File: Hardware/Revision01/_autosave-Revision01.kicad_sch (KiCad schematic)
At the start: 24 parts, among them J1 Battery connector, SW1 ON/OFF_SW_SPST_LED, U1 NUCLEO-L476RG

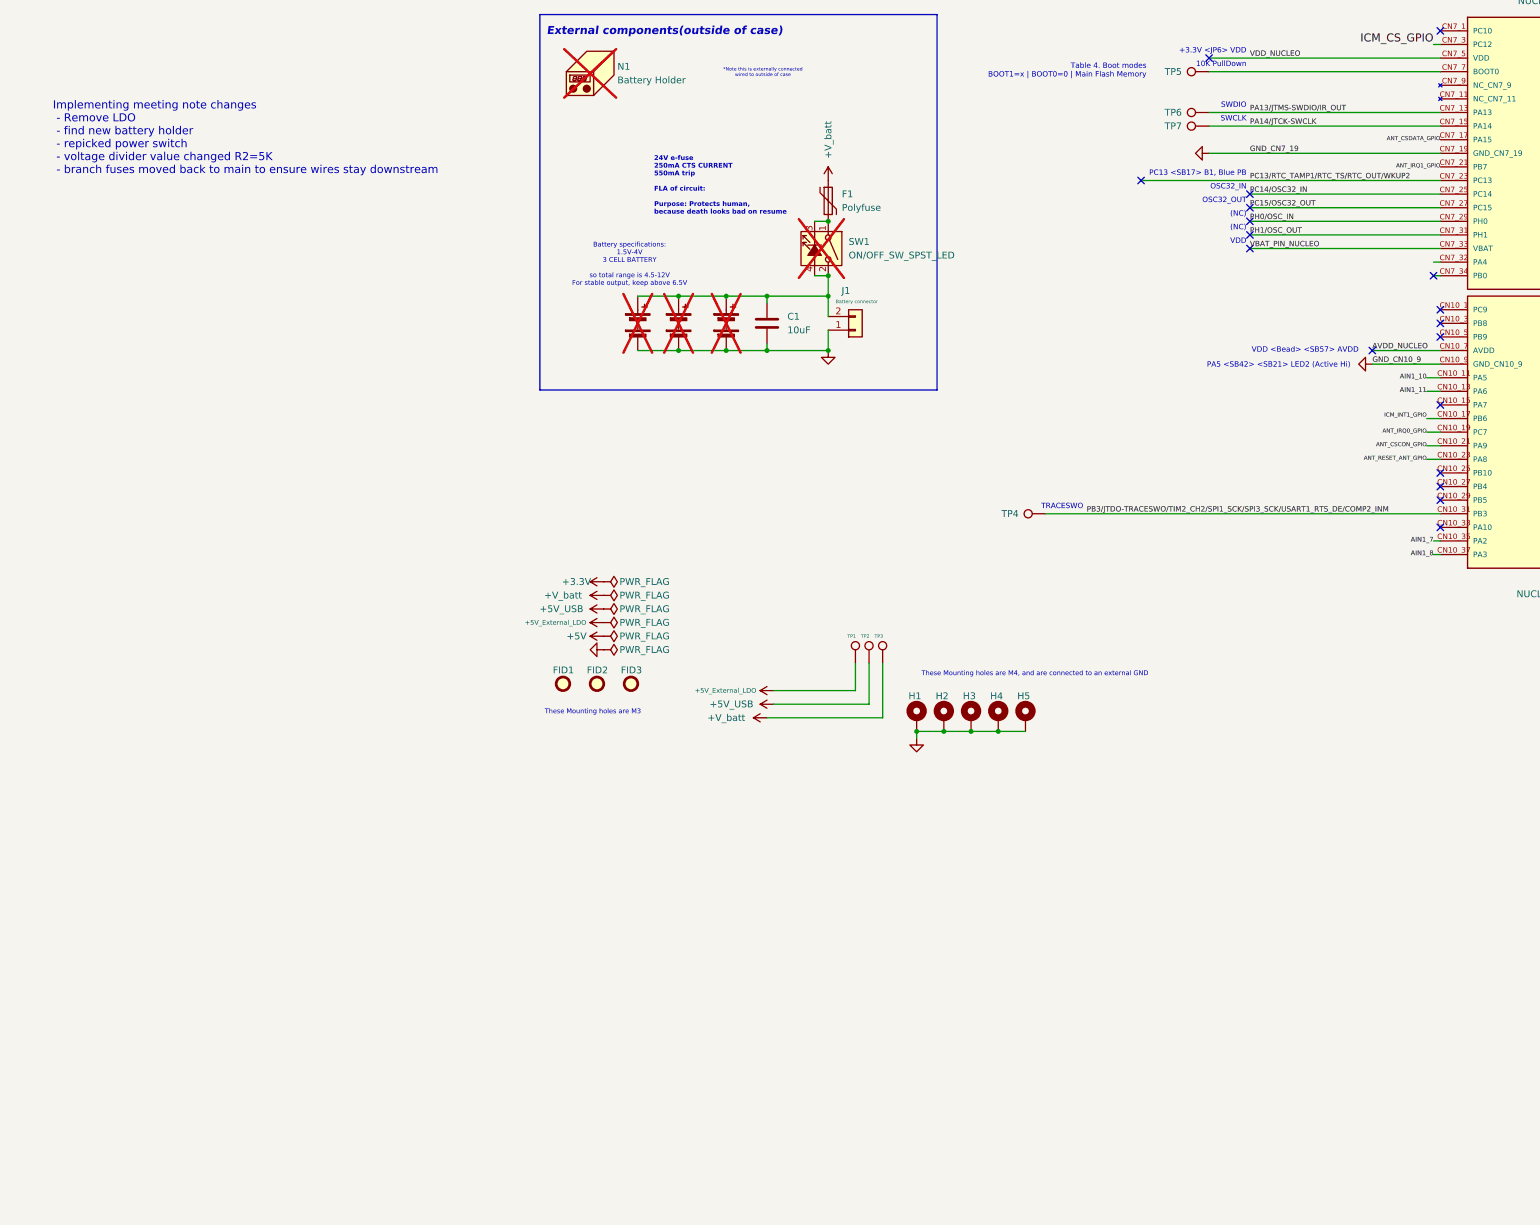
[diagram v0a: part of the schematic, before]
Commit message: Small details on PART B, restarting component placement on PART A
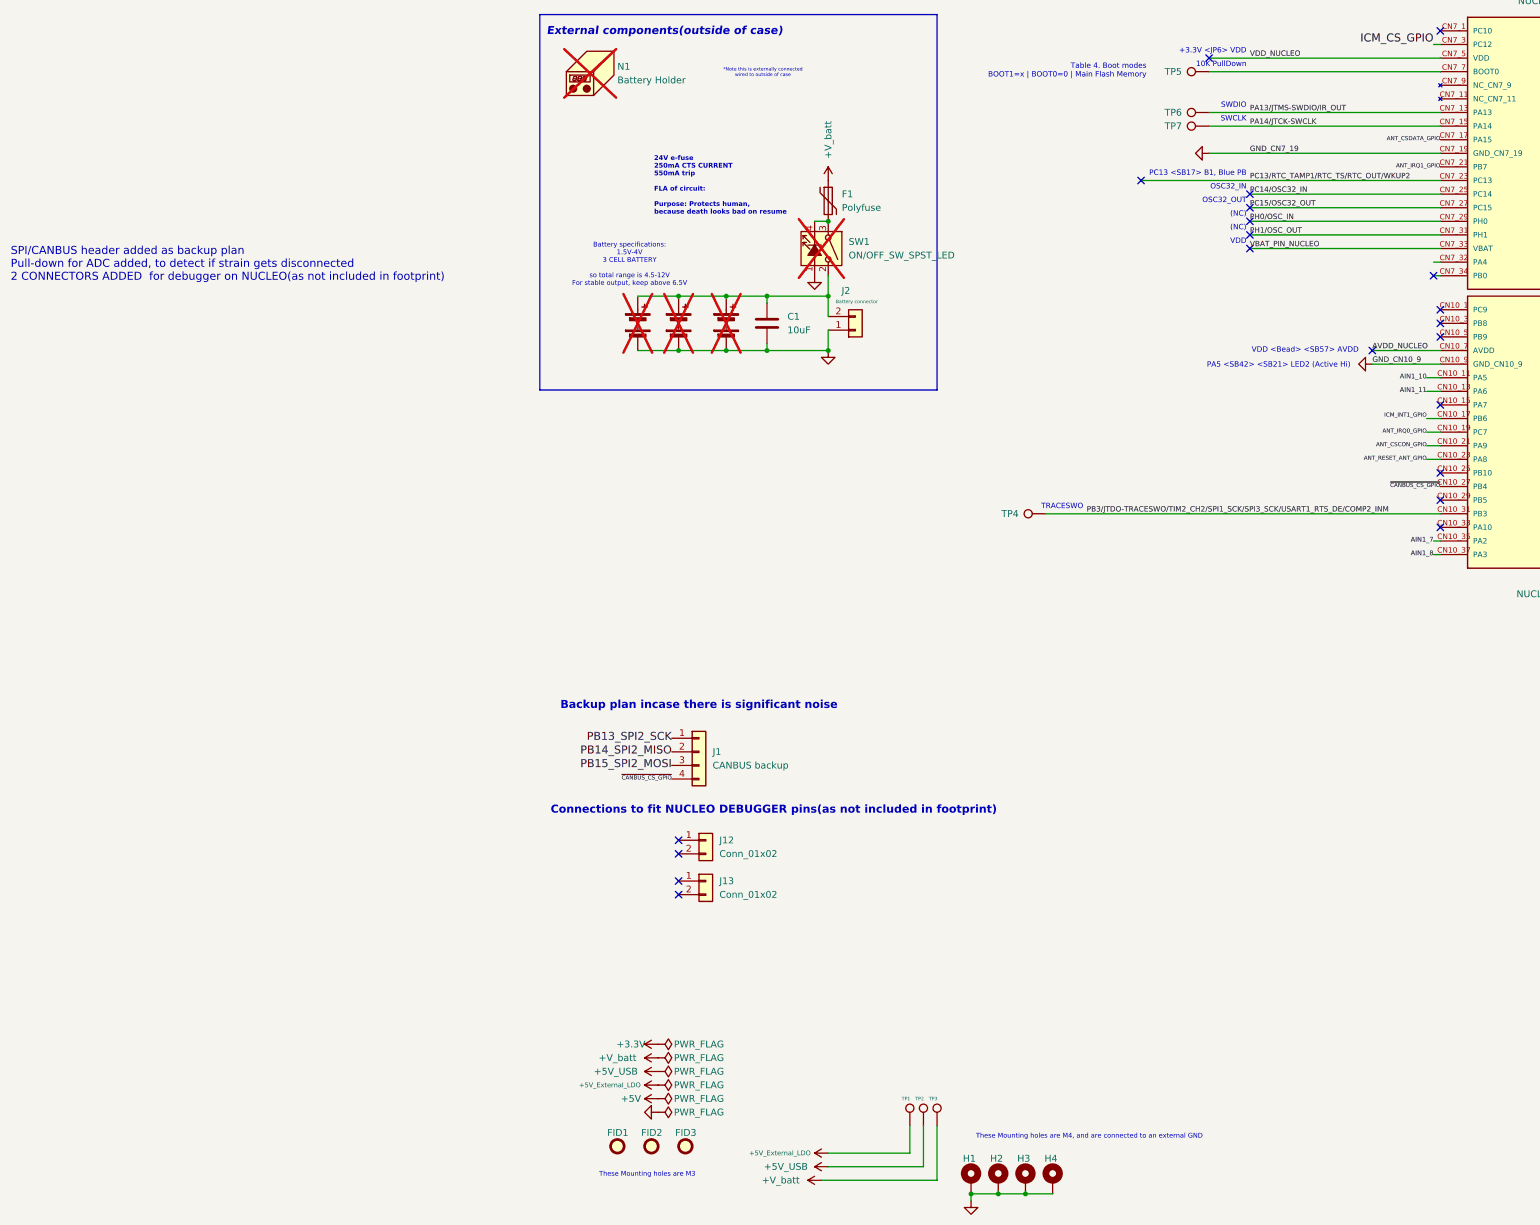
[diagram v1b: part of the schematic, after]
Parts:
- removed H5: MountingHole_Pad_MP, MountingHole:MountingHole_4.3mm_M4_ISO7380_Pad_TopBottom, symbol Mechanical:MountingHole_Pad_MP
- added J1: CANBUS backup, Connector_PinHeader_2.54mm:PinHeader_1x04_P2.54mm_Vertical, symbol Connector_Generic:Conn_01x04
- added J12, J13: Conn_01x02, Connector_PinHeader_2.54mm:PinHeader_1x02_P2.54mm_Vertical, symbol Connector_Generic:Conn_01x02
- renumbered J1 to J2
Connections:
- net GND: now also SW1.1
- net PB13_SPI2_SCK: now also J1.1 (Pin_1)
- net PB14_SPI2_MISO: now also J1.2 (Pin_2)
- net PB15_SPI2_MOSI: now also J1.3 (Pin_3)
- net at BT1.1 (+), BT2.1 (+), BT3.1 (+)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: no longer SW1.4 (A)
- net ~{CANBUS_CS_GPIO}: now reaches U1.CN10_27 (PB4)
- net ~{CANBUS_CS_GPIO}: now also J1.4 (Pin_4)
- net at F1.2, SW1.3 (K): now also SW1.4 (A); no longer SW1.1
- no-connect marks 29 -> 32
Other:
- note added: "Backup plan incase there is significant noise"
- note added: "Connections to fit NUCLEO DEBUGGER pins(as not included in footprint)"
- note added: "SPI/CANBUS header added as backup plan Pull-down for ADC added, to detect if strain gets disconnected 2 CONNECTORS ADDED for debugger on NUCLEO(as not included in footprint)"
- note removed: "Implementing meeting note changes - Remove LDO - find new battery holder - repicked power switch - voltage divider value changed R2=5K - branch fuses moved back to main to ensure wires stay downstream"
- moved on the sheet: FID1, FID2, FID3, H1, H2, H3, H4, TP1, TP2, TP3
